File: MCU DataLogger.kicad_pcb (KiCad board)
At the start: 2 copper layers, 27 parts, among them J1 Conn_01x04_Pin, J2 Conn_01x09_Pin, J3 Conn_01x04_Pin, J4 Conn_02x03_Odd_Even, U3 DS1337S_, U4 ATMEGA328P-AU, Y1 32.768 KH, Y2 16MHz

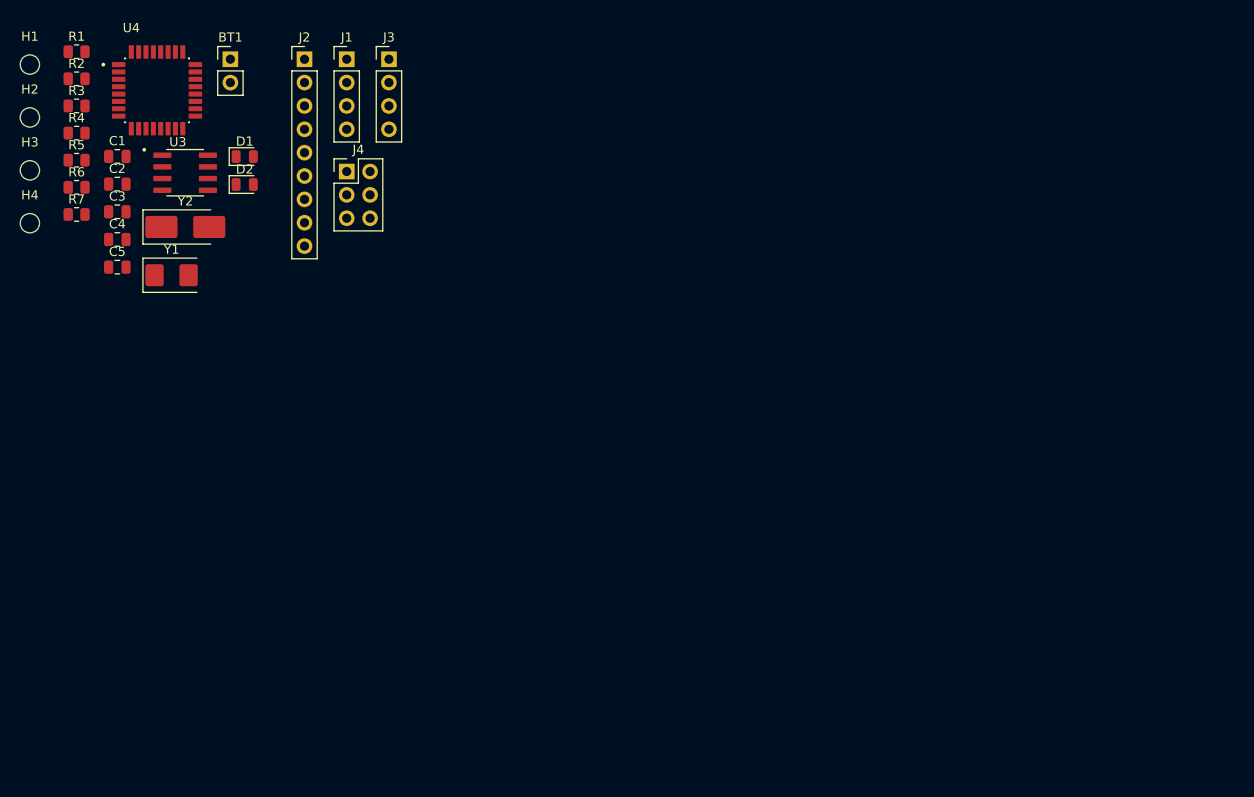
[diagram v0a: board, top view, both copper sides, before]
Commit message: Added the footprint to U1 and U2, staging for pcb schematic import and layout
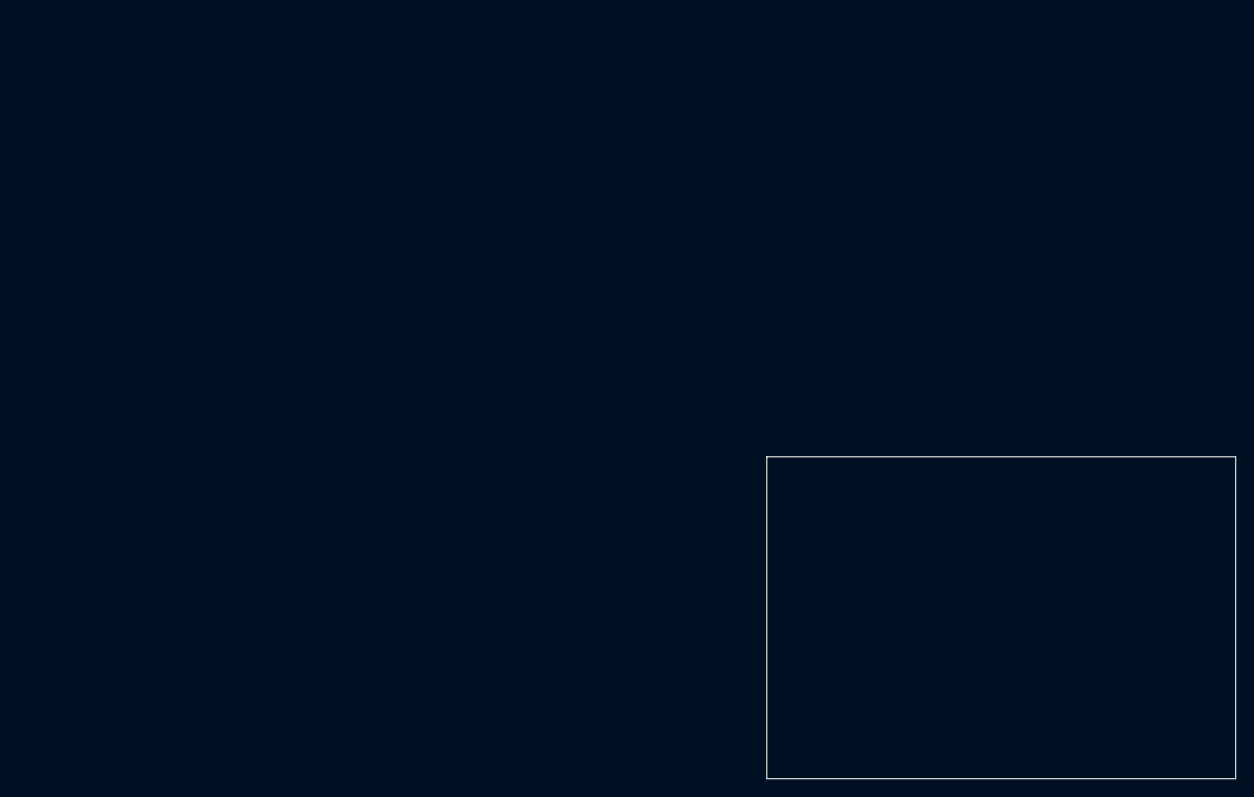
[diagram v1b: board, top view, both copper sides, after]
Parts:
- removed BT1: Battery, Connector_PinHeader_2.54mm:PinHeader_1x02_P2.54mm_Vertical
- removed C1, C4: 0.1uF, Capacitor_SMD:C_0805_2012Metric
- removed C2, C3: 22pF, Capacitor_SMD:C_0805_2012Metric
- removed C5: 100nF, Capacitor_SMD:C_0805_2012Metric
- removed D1, D2: LED, LED_SMD:LED_0805_2012Metric
- removed H1, H2, H3, H4: MountingHole, MountingHole:MountingHole_2.1mm
- removed J1, J3: Conn_01x04_Pin, Connector_PinHeader_2.54mm:PinHeader_1x04_P2.54mm_Vertical
- removed J2: Conn_01x09_Pin, Connector_PinHeader_2.54mm:PinHeader_1x09_P2.54mm_Vertical
- removed J4: Conn_02x03_Odd_Even, Connector_PinHeader_2.54mm:PinHeader_2x03_P2.54mm_Vertical
- removed R1, R6: 10K, Resistor_SMD:R_0805_2012Metric
- removed R2: 10k, Resistor_SMD:R_0805_2012Metric
- removed R3, R4: 4.7K, Resistor_SMD:R_0805_2012Metric
- removed R5, R7: 330, Resistor_SMD:R_0805_2012Metric
- removed U3: DS1337S_, Footprints:SOIC127P600X175-8N
- removed U4: ATMEGA328P-AU, Footprints:QFP80P900X900X120-32N
- removed Y1: 32.768 KH, Crystal:Crystal_SMD_5032-2Pin_5.0x3.2mm
- removed Y2: 16MHz, Crystal:Crystal_SMD_5032-2Pin_5.0x3.2mm_HandSoldering
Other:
- board outline added: 51 x 35 mm

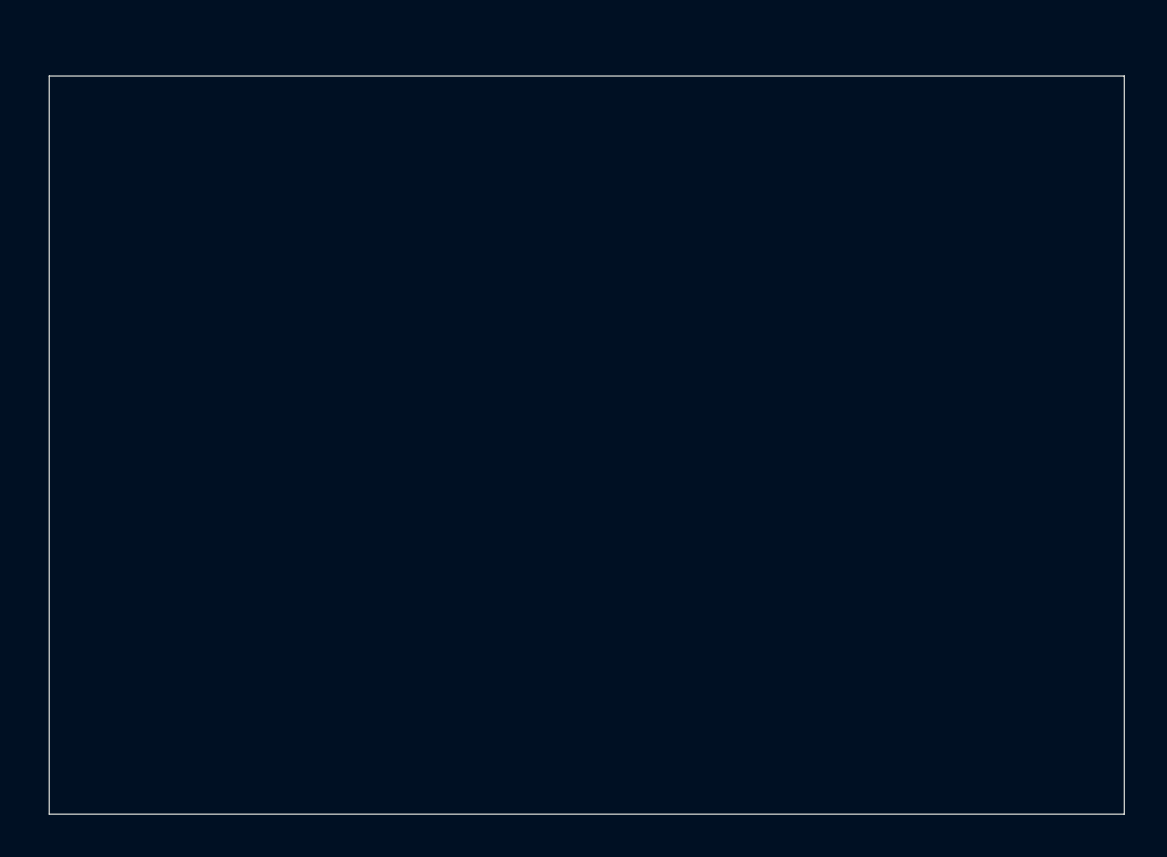
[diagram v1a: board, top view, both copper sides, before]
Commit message: Completed the laout of the footprints in the pcb layer
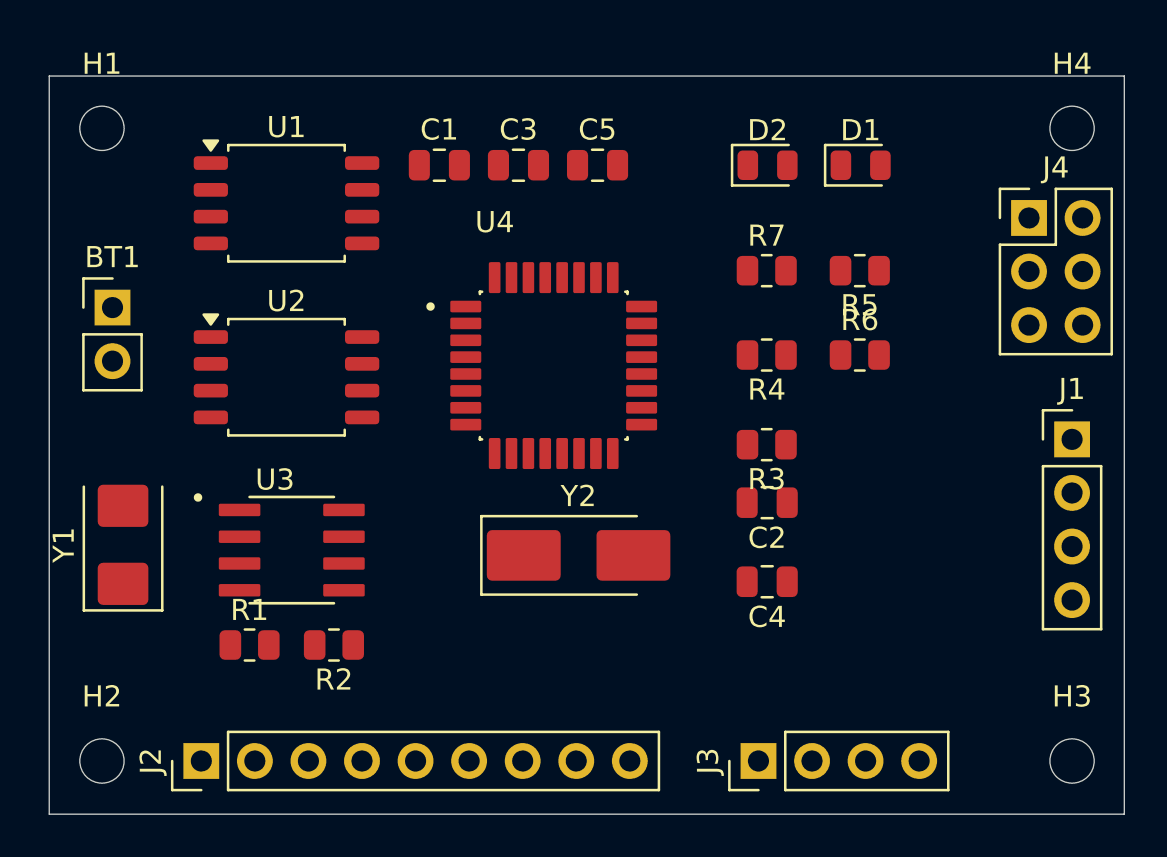
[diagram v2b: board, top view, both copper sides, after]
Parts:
- added BT1: Battery, Connector_PinHeader_2.54mm:PinHeader_1x02_P2.54mm_Vertical, F.Cu at (103.0, 71.0)
- added C1: 0.1uF, Capacitor_SMD:C_0805_2012Metric, F.Cu at (118.5, 64.2)
- added C2: 22pF, Capacitor_SMD:C_0805_2012Metric, F.Cu at (134.0, 80.2)
- added C3: 22pF, Capacitor_SMD:C_0805_2012Metric, F.Cu at (122.2, 64.2)
- added C4: 0.1uF, Capacitor_SMD:C_0805_2012Metric, F.Cu at (134.0, 84.0)
- added C5: 100nF, Capacitor_SMD:C_0805_2012Metric, F.Cu at (126.0, 64.2)
- added D1: LED, LED_SMD:LED_0805_2012Metric, F.Cu at (138.5, 64.2)
- added D2: LED, LED_SMD:LED_0805_2012Metric, F.Cu at (134.1, 64.2)
- added H1: MountingHole, MountingHole:MountingHole_2.1mm, F.Cu at (102.5, 62.5)
- added H2: MountingHole, MountingHole:MountingHole_2.1mm, F.Cu at (102.5, 92.5)
- added H3: MountingHole, MountingHole:MountingHole_2.1mm, F.Cu at (148.5, 92.5)
- added H4: MountingHole, MountingHole:MountingHole_2.1mm, F.Cu at (148.5, 62.5)
- added J1: Conn_01x04_Pin, Connector_PinHeader_2.54mm:PinHeader_1x04_P2.54mm_Vertical, F.Cu at (148.5, 77.2)
- added J2: Conn_01x09_Pin, Connector_PinHeader_2.54mm:PinHeader_1x09_P2.54mm_Vertical, F.Cu at (107.2, 92.5)
- added J3: Conn_01x04_Pin, Connector_PinHeader_2.54mm:PinHeader_1x04_P2.54mm_Vertical, F.Cu at (133.6, 92.5)
- added J4: Conn_02x03_Odd_Even, Connector_PinHeader_2.54mm:PinHeader_2x03_P2.54mm_Vertical, F.Cu at (146.5, 66.8)
- added R1: 10K, Resistor_SMD:R_0805_2012Metric, F.Cu at (109.5, 87.0)
- added R2: 10k, Resistor_SMD:R_0805_2012Metric, F.Cu at (113.5, 87.0)
- added R3: 4.7K, Resistor_SMD:R_0805_2012Metric, F.Cu at (134.0, 77.5)
- added R4: 4.7K, Resistor_SMD:R_0805_2012Metric, F.Cu at (134.0, 73.2)
- added R5: 330, Resistor_SMD:R_0805_2012Metric, F.Cu at (138.4, 69.2)
- added R6: 10K, Resistor_SMD:R_0805_2012Metric, F.Cu at (138.4, 73.2)
- added R7: 330, Resistor_SMD:R_0805_2012Metric, F.Cu at (134.0, 69.2)
- added U1: 24LC1025, Package_SO:SOIC-8_5.3x5.3mm_P1.27mm, F.Cu at (111.2, 66.1)
- added U2: 24LC1025, Package_SO:SOIC-8_5.3x5.3mm_P1.27mm, F.Cu at (111.2, 74.3)
- added U3: DS1337S_, Footprints:SOIC127P600X175-8N, F.Cu at (111.5, 82.5)
- added U4: ATMEGA328P-AU, Footprints:QFP80P900X900X120-32N, F.Cu at (123.9, 73.8)
- added Y1: 32.768 KH, Crystal:Crystal_SMD_5032-2Pin_5.0x3.2mm, F.Cu at (103.5, 82.2)
- added Y2: 16MHz, Crystal:Crystal_SMD_5032-2Pin_5.0x3.2mm_HandSoldering, F.Cu at (125.1, 82.8)

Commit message: Resolved all the unconnected erc errors and assigned the propper cadd model for U2 and U4
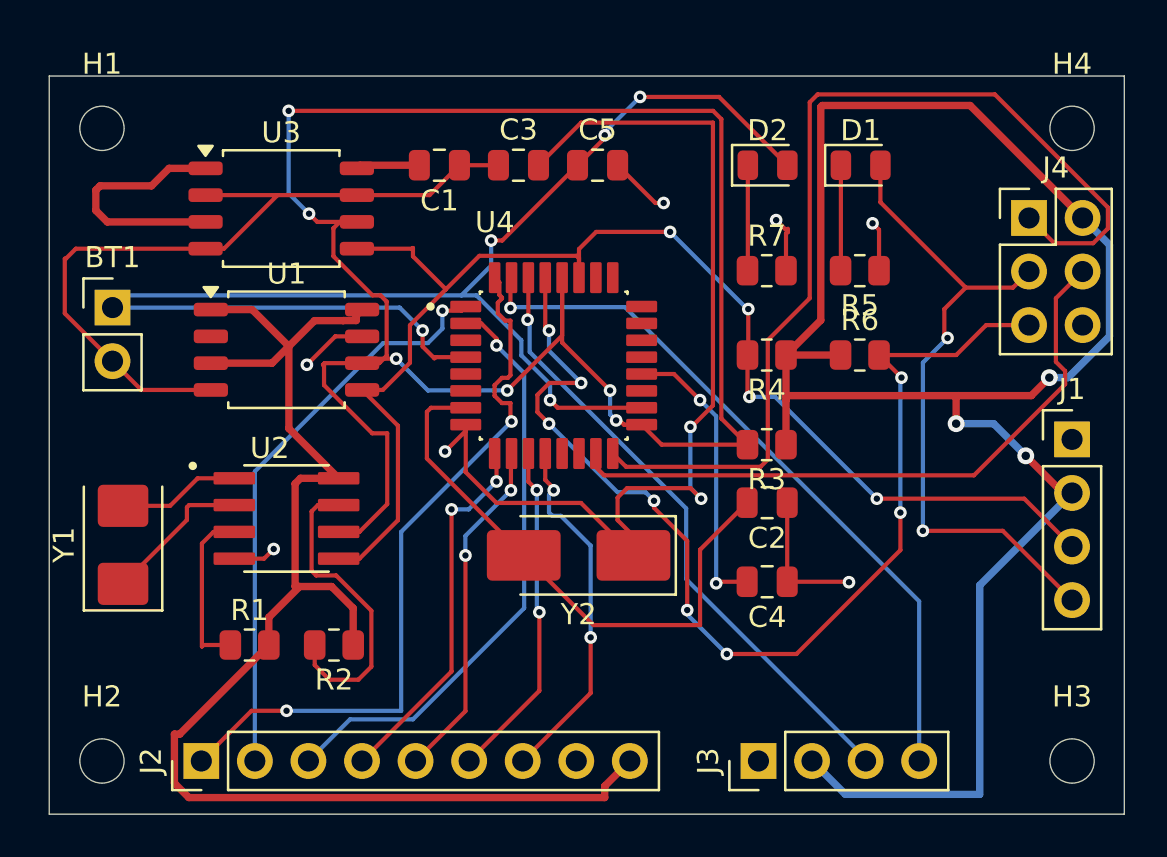
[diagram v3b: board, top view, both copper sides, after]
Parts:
- U2: value 24LC1025 -> DS1337S_; footprint Package_SO:SOIC-8_5.3x5.3mm_P1.27mm -> Footprints:SOIC127P600X175-8N
- U3: value DS1337S_ -> 24LC1025; footprint Footprints:SOIC127P600X175-8N -> Package_SO:SOIC-8_5.3x5.3mm_P1.27mm
- moved U3 16.2 mm to (111.0, 66.3)
- moved U1 6.95 mm to (111.2, 73.0)
- moved U2 6.70 mm to (111.2, 81.0)
- turned C1 to 180 degrees
- turned Y2 to 180 degrees
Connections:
- D1 pad 2: Net-(BT1-+) -> /SCK
- D2 pad 2: /SCK -> Net-(BT1-+)
- R1 pad 1: Net-(U3-~{INTA}) -> Net-(U2-~{INTA})
- R2 pad 2: Net-(U3-SQW/~INT) -> Net-(U2-SQW/~INT)
- R5 pad 2: Net-(D2-K) -> Net-(D1-K)
- R7 pad 1: Net-(D1-K) -> Net-(D2-K)
- U2 pad 1: /Vcc -> Net-(U2-X1)
- U2 pad 2: GND -> Net-(U2-X2)
- U2 pad 3: /Vcc -> Net-(U2-~{INTA})
- U2 pad 7: GND -> Net-(U2-SQW/~INT)
- U3 pad 1: Net-(U3-X1) -> /Vcc
- U3 pad 2: Net-(U3-X2) -> GND
- U3 pad 3: Net-(U3-~{INTA}) -> /Vcc
- U3 pad 7: Net-(U3-SQW/~INT) -> GND
- Y1 pad 1: Net-(U3-X2) -> Net-(U2-X2)
- Y1 pad 2: Net-(U3-X1) -> Net-(U2-X1)
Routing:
- net /Vcc: track 0.00 -> 172.0 mm, vias 0 -> 3
- net /SCK: track 0.00 -> 127.5 mm, vias 0 -> 8
- net Net-(BT1-+): track 0.00 -> 68.2 mm, vias 0 -> 5
- net /SDA: track 0.00 -> 64.3 mm, vias 0 -> 4
- net GND: track 0.00 -> 56.9 mm, vias 0 -> 6
- net /RESET: track 0.00 -> 52.5 mm, vias 0 -> 8
- net Net-(U4-PB7): track 0.00 -> 48.6 mm, vias 0 -> 3
- net /MISO: track 0.00 -> 47.6 mm
- net /D2: track 0.00 -> 34.8 mm, vias 0 -> 2
- net /TX: track 0.00 -> 34.2 mm, vias 0 -> 1
- net /MOSI: track 0.00 -> 30.9 mm
- net /RX: track 0.00 -> 29.6 mm, vias 0 -> 1
- net /D4: track 0.00 -> 28.3 mm, vias 0 -> 1
- net /D3: track 0.00 -> 27.5 mm, vias 0 -> 1
- net Net-(U4-PB6): track 0.00 -> 27.1 mm
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
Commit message: Added copper fill and connected the floating vcc pins and resolved some unconnected GND surface level pins
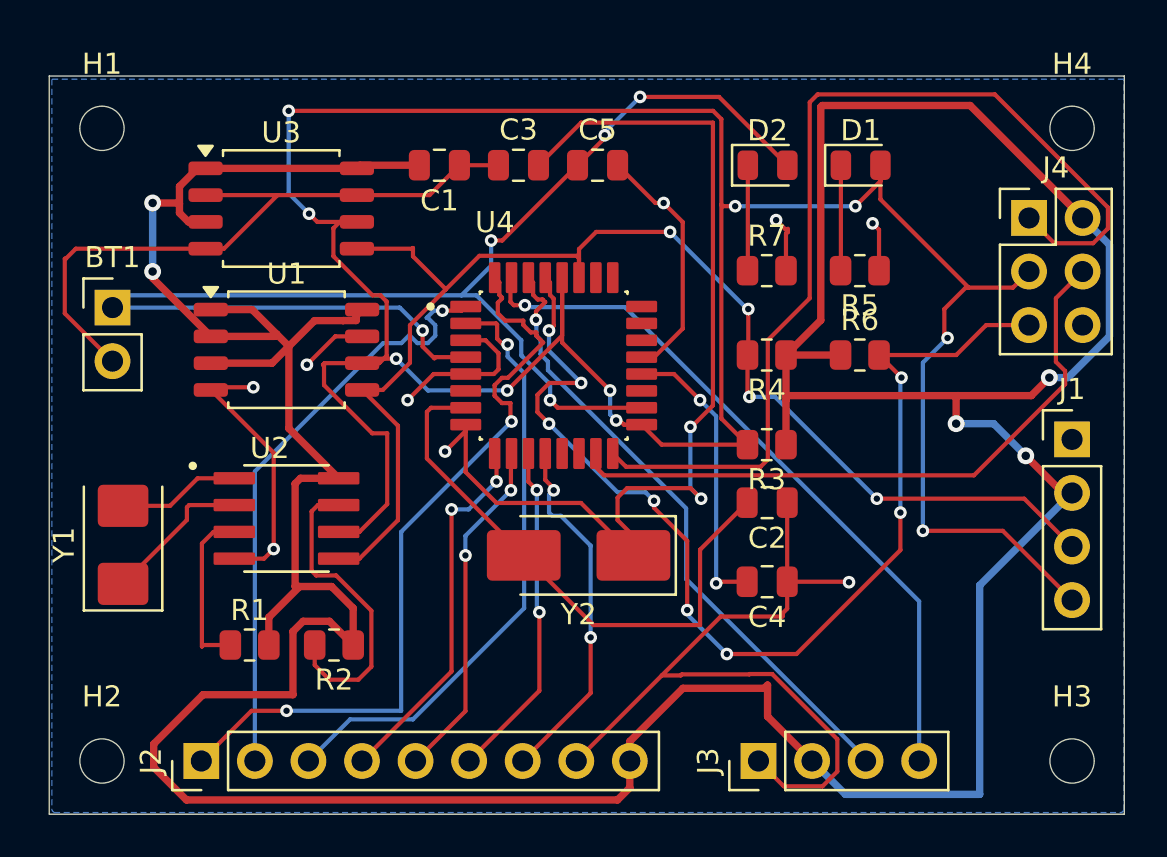
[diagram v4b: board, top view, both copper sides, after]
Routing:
- net GND: track 56.9 -> 108.9 mm, vias 6 -> 8
- net /Vcc: track 172.0 -> 204.8 mm, vias 3 -> 5
- net /SCK: track 127.5 -> 136.4 mm, vias 8 -> 10
- net /D2: track 34.8 -> 36.6 mm
- net /D3: track 27.5 -> 28.4 mm
- net /RX: track 29.6 -> 30.3 mm
- net /D4: track 28.3 -> 28.9 mm
- added copper zone on B.Cu, net GND

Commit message: Fixed the warnings in the pcb editor from the erc check
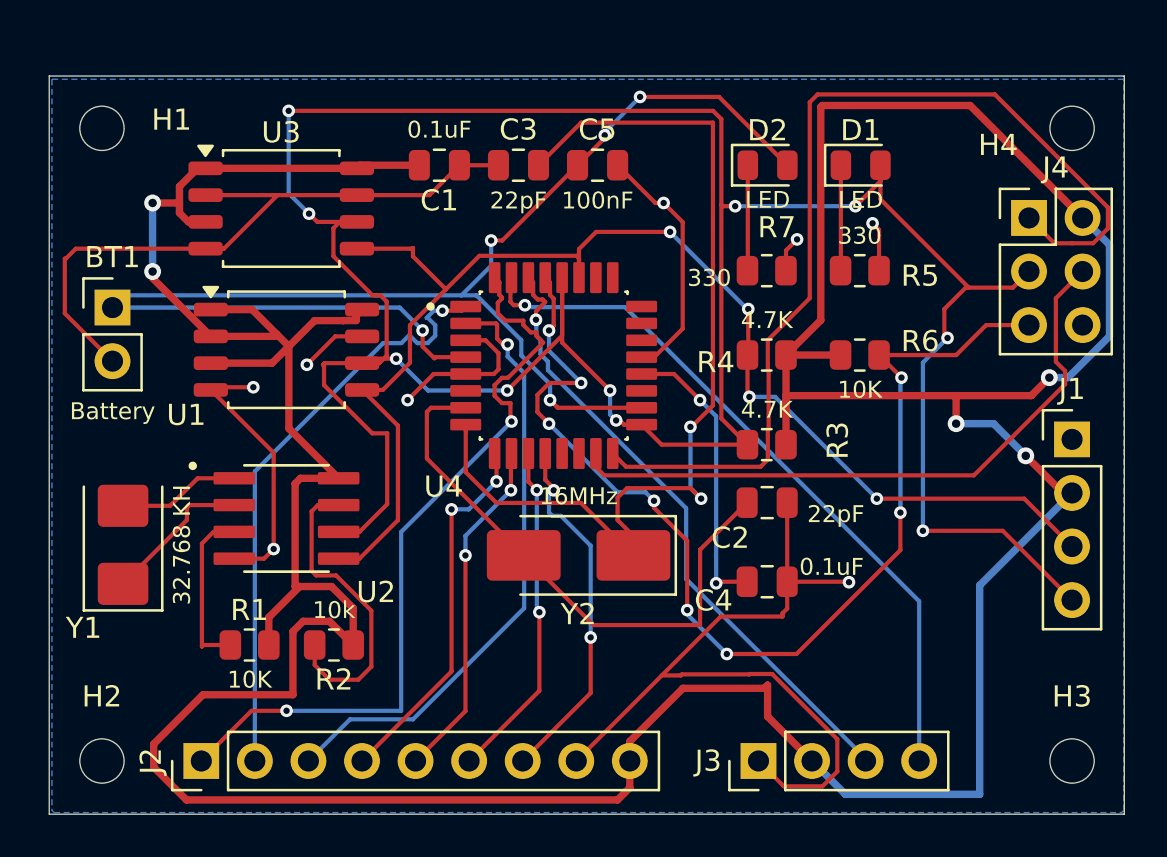
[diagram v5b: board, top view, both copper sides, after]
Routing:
- net Net-(U4-PB7): track 48.6 -> 47.2 mm, vias 3 -> 2
- net GND: track 108.9 -> 107.8 mm
